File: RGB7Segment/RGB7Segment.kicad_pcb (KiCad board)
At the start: 2 copper layers, 35.2 x 21.4 mm, 32 parts, among them J1 Conn_01x02_Socket, J2 Conn_01x04_Pin

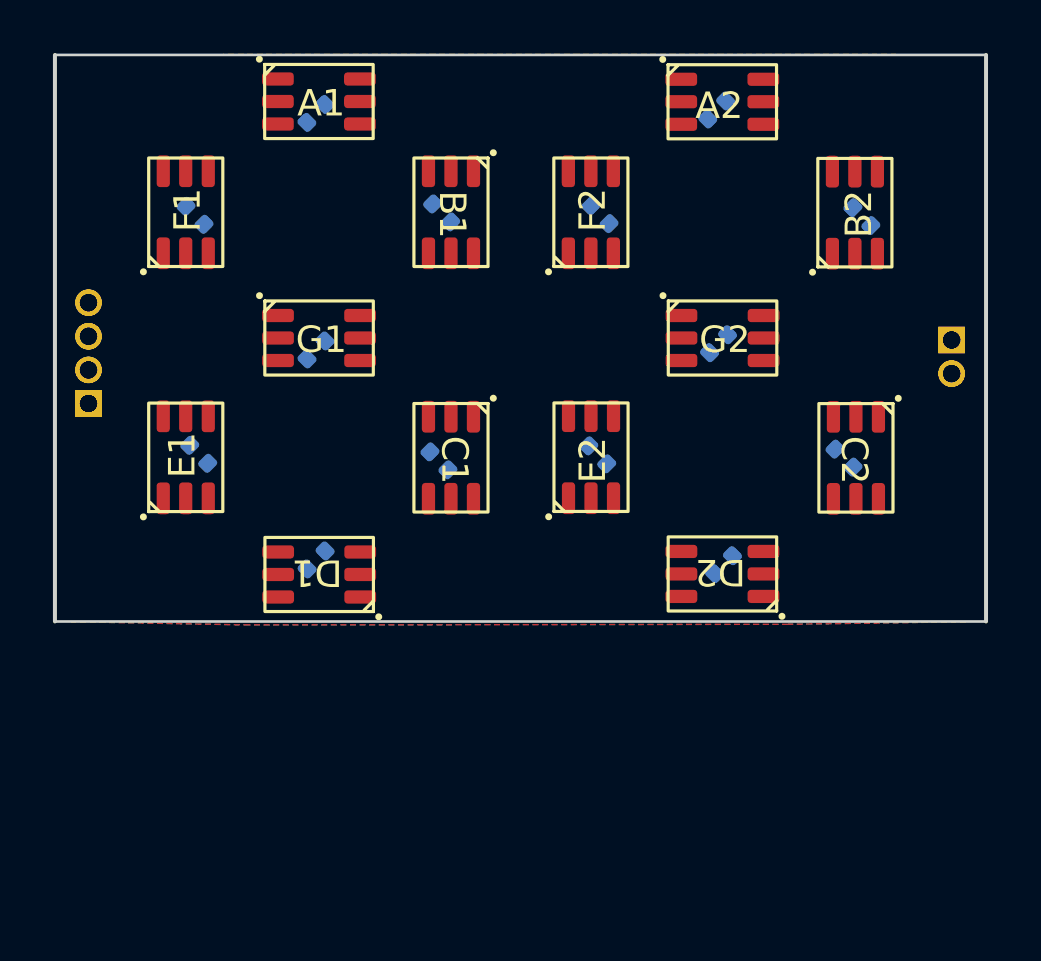
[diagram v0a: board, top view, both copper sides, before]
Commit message: Routing Complete
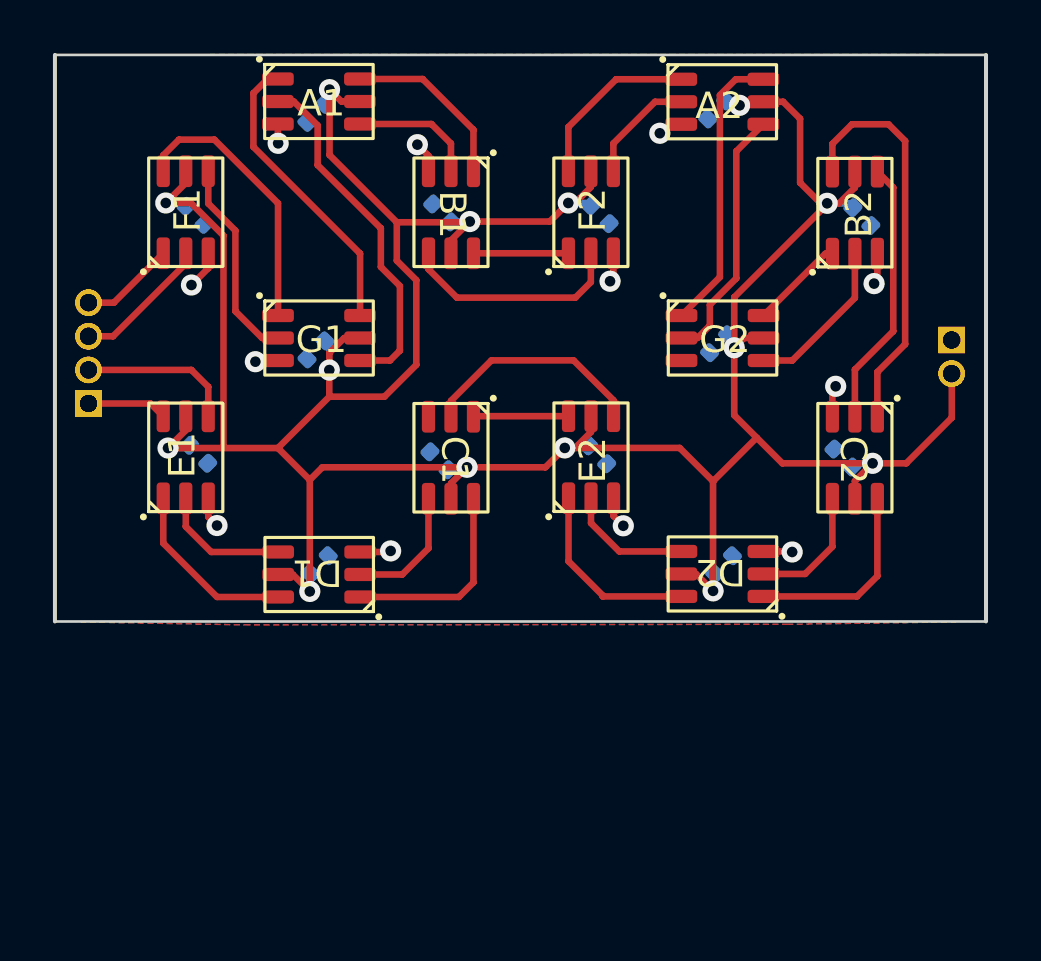
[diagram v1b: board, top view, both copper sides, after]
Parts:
- moved C12 0.21 mm to (226.9, 114.4)
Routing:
- net VCC: track 0.00 -> 128.6 mm, vias 0 -> 14
- net /B2_DO: track 0.00 -> 15.2 mm
- net /G1_CO: track 0.00 -> 13.3 mm
- net GND: track 0.00 -> 13.3 mm, vias 0 -> 12
- net /G1_DO: track 0.00 -> 11.2 mm
- net /A2_DO: track 0.00 -> 10.8 mm
- net /F1_DO: track 0.00 -> 10.4 mm
- net /B2_CO: track 0.00 -> 10.1 mm
- net /A2_CO: track 0.00 -> 9.71 mm
- net /E2_CO: track 0.00 -> 8.60 mm
- net /B1_CO: track 0.00 -> 8.51 mm
- net /F1_CO: track 0.00 -> 7.74 mm
- net /C1_DO: track 0.00 -> 7.67 mm
- net /C2_DO: track 0.00 -> 7.54 mm
- net /D2_DO: track 0.00 -> 7.22 mm
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
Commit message: Adding Vias
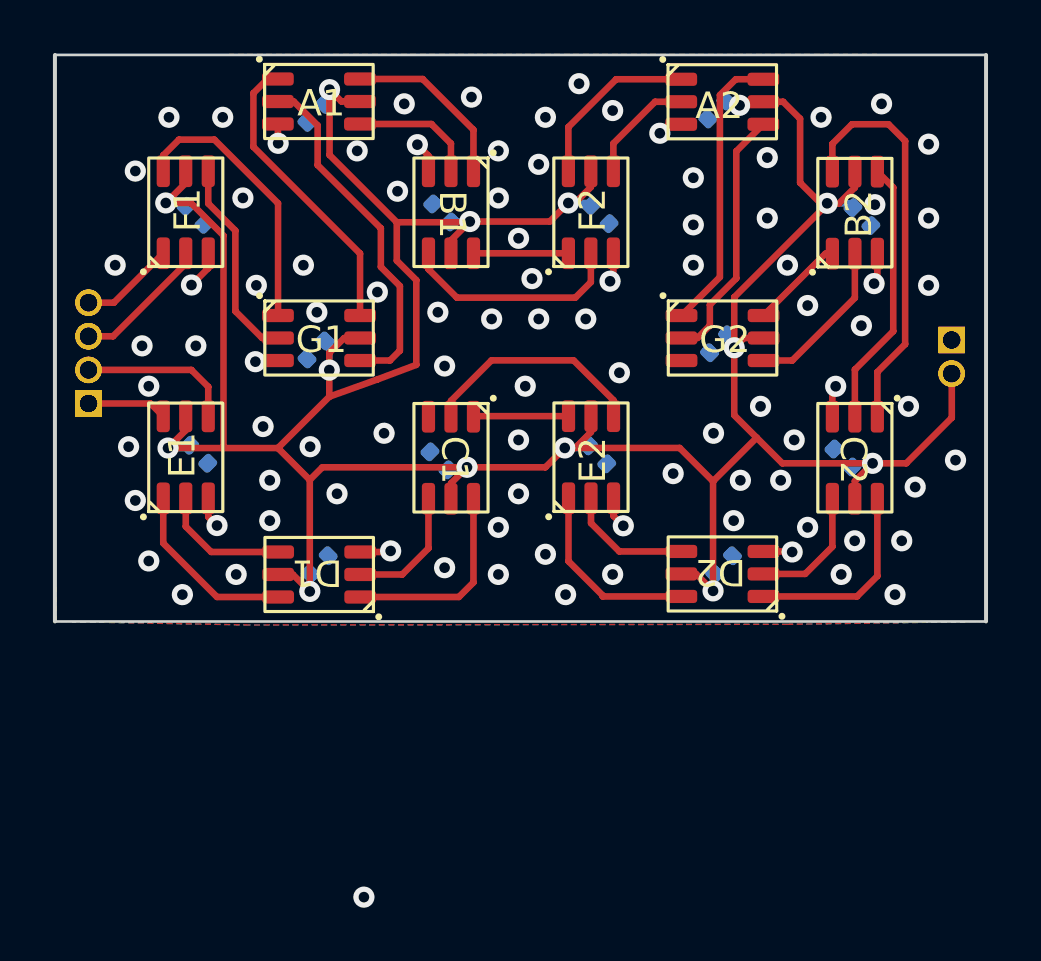
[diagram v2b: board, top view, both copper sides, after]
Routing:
- net GND: vias 12 -> 92

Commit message: Ordered Board
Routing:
- net /B2_DO: track 15.2 -> 13.8 mm
- net GND: vias 92 -> 85
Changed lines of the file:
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@@
 	)
 	(gr_text "DOUT"
-		(at 220.6 109.3 180)
+		(at 219.583 107.6198 180)
 		(layer "B.SilkS")
 		(effects
@@
 	)
 	(gr_text "DIN"
-		(at 219.75 102.75 180)
+		(at 219.310044 103.845537 180)
 		(layer "B.SilkS")
 		(effects
@@
 	)
 	(segment
+		(start 220.066527 102.674055)
+		(end 221.019411 102.674055)
+		(width 0.25)
+		(layer "F.Cu")
+		(net 2)
+	)
+	(segment
 		(start 218.200044 104.540538)
-		(end 219.152928 104.540538)
-		(width 0.25)
-		(layer "F.Cu")
-		(net 2)
-	)
-	(segment
-		(start 219.152928 104.540538)
-		(end 221.019411 102.674055)
+		(end 220.066527 102.674055)
 		(width 0.25)
 		(layer "F.Cu")
@@
 	)
 	(via
-		(at 242.824 111.252)
+		(at 243.0018 111.4806)
 		(size 0.8)
 		(drill 0.4)
@@
 	)
 	(via
-		(at 244.602 103.124)
-		(size 0.8)
-		(drill 0.4)
-		(layers "F.Cu" "B.Cu")
-		(free yes)
-		(net 3)
-	)
-	(via
 		(at 237.9 103.73)
 		(size 0.8)
@@
 	)
 	(via
-		(at 219.964 112.014)
+		(at 219.8116 111.9886)
 		(size 0.8)
 		(drill 0.4)
@@
 	)
 	(via
-		(at 247.904 100.838)
-		(size 0.8)
-		(drill 0.4)
-		(layers "F.Cu" "B.Cu")
-		(free yes)
-		(net 3)
-	)
-	(via
 		(at 226.314 103.124)
 		(size 0.8)
@@
 	)
 	(via
-		(at 234.442 102.108)
-		(size 0.8)
-		(drill 0.4)
-		(layers "F.Cu" "B.Cu")
-		(free yes)
-		(net 3)
-	)
-	(via
 		(at 249.428 111.506)
 		(size 0.8)
@@
 	)
 	(via
-		(at 219.202 103.124)
-		(size 0.8)
-		(drill 0.4)
-		(layers "F.Cu" "B.Cu")
-		(free yes)
-		(net 3)
-	)
-	(via
-		(at 234.95 103.632)
+		(at 234.442 103.4796)
 		(size 0.8)
 		(drill 0.4)
@@
 	)
 	(via
-		(at 244.856 109.728)
+		(at 244.8814 109.601)
 		(size 0.8)
 		(drill 0.4)
@@
 	)
 	(via
-		(at 220.472 107.696)
-		(size 0.8)
-		(drill 0.4)
-		(layers "F.Cu" "B.Cu")
-		(free yes)
-		(net 3)
-	)
-	(via
 		(at 231.394 104.902)
 		(size 0.8)
@@
 	)
 	(via
-		(at 229.108 104.14)
-		(size 0.8)
-		(drill 0.4)
-		(layers "F.Cu" "B.Cu")
-		(free yes)
-		(net 3)
-	)
-	(via
 		(at 225.044 112.776)
 		(size 0.8)
@@
 	)
 	(via
-		(at 228.6 127)
-		(size 0.8)
-		(drill 0.4)
-		(layers "F.Cu" "B.Cu")
-		(free yes)
-		(net 3)
-	)
-	(via
 		(at 226.568 109.982)
 		(size 0.8)
@@
 	)
 	(via
-		(at 244.348 111.252)
+		(at 244.3734 111.6584)
 		(size 0.8)
 		(drill 0.4)
@@
 	)
 	(via
-		(at 220.472 114.3)
+		(at 220.1418 114.2238)
 		(size 0.8)
 		(drill 0.4)
@@
 	)
 	(segment
-		(start 246.299767 98.540233)
-		(end 246.299767 99.589411)
+		(start 246.299767 98.989412)
+		(end 246.624768 98.664411)
 		(width 0.25)
 		(layer "F.Cu")
@@
 	)
 	(segment
-		(start 247.04 97.8)
-		(end 246.299767 98.540233)
-		(width 0.25)
-		(layer "F.Cu")
-		(net 14)
-	)
-	(segment
-		(start 249.049767 106.110233)
-		(end 249.049767 98.429767)
-		(width 0.25)
-		(layer "F.Cu")
-		(net 14)
-	)
-	(segment
-		(start 249.049767 98.429767)
-		(end 248.42 97.8)
+		(start 248.577978 98.664411)
+		(end 249.049767 99.1362)
 		(width 0.25)
 		(layer "F.Cu")
@@
 	)
 	(segment
-		(start 248.42 97.8)
-		(end 247.04 97.8)
+		(start 246.299767 99.589411)
+		(end 246.299767 98.989412)
 		(width 0.25)
 		(layer "F.Cu")
@@
 		(width 0.25)
 		(layer "F.Cu")
+		(net 14)
+	)
+	(segment
+		(start 246.624768 98.664411)
+		(end 248.577978 98.664411)
+		(width 0.25)
+		(layer "F.Cu")
+		(net 14)
+	)
+	(segment
+		(start 249.049767 106.110233)
+		(end 249.049767 99.1362)
+		(width 0.25)
+		(layer "F.Cu")
